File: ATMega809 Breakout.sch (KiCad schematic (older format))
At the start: 42 parts, among them J1 USB_B_Micro, J2 Conn_01x05, J3 Conn_01x20, J4 Conn_01x12, J5 UPDI, Q1 PJA3438-AU, Q2 PJA3438-AU, Q3 PJA3438-AU, Q4 PJA3438-AU, Q5 PJA3438-AU, SW1 RESET, U1 NCP1117-ADJ_SOT223, U2 ATMEGA809-AF

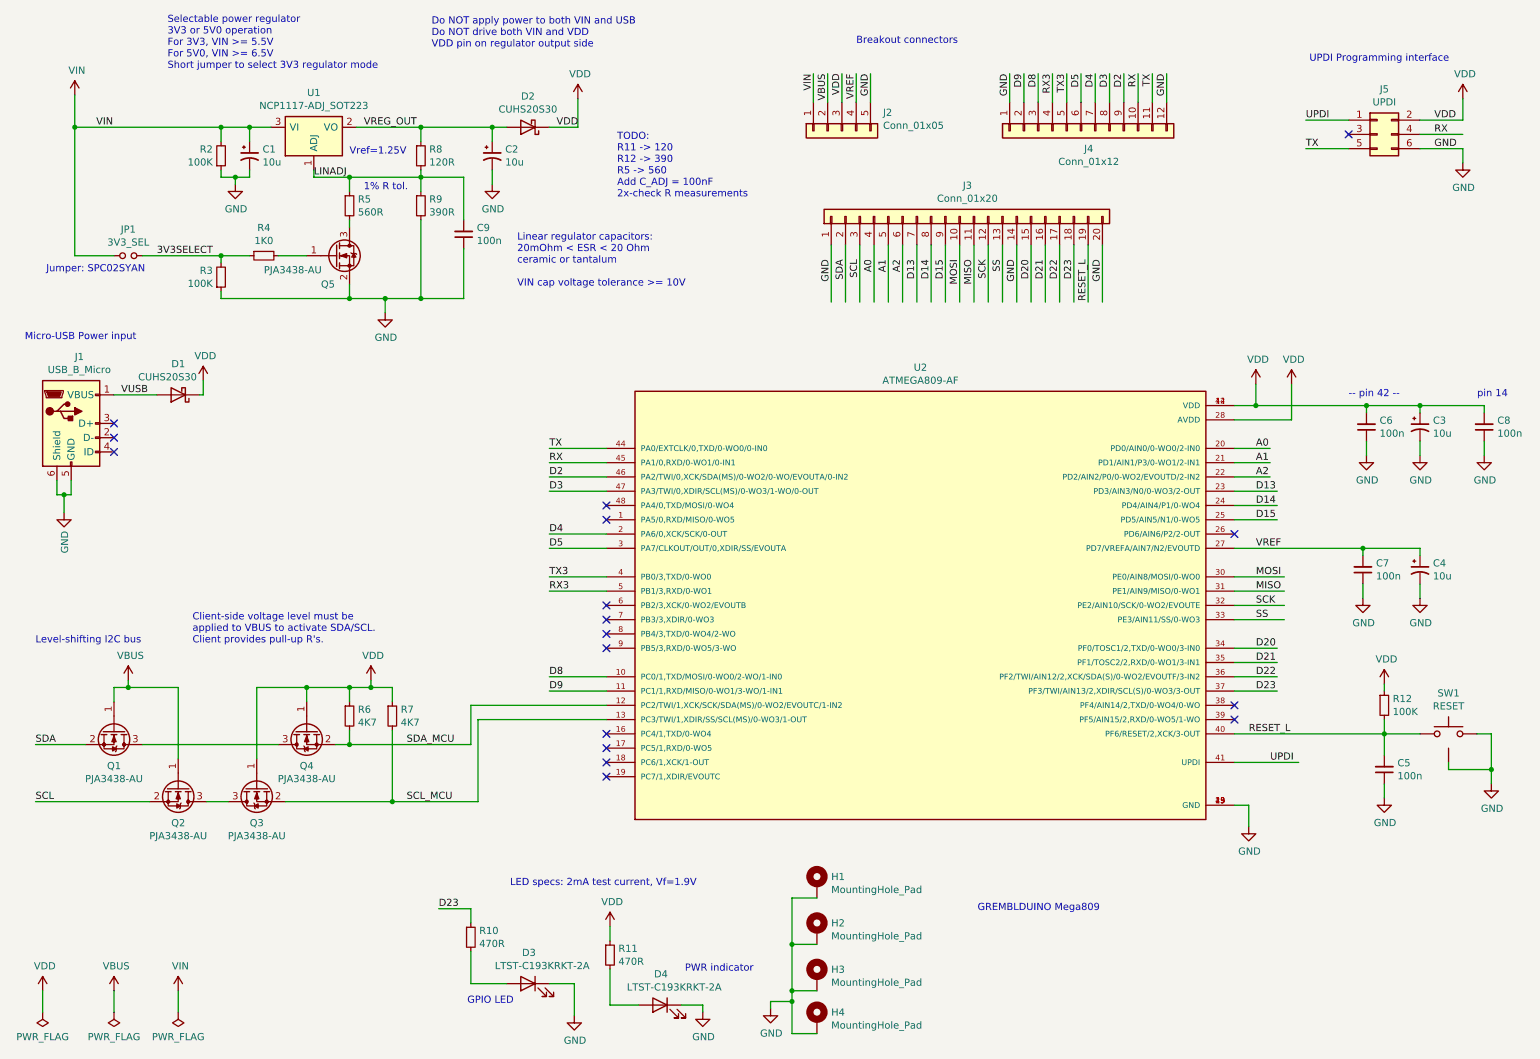
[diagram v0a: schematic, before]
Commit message: Cleanup. Basically ready for mfg.
* Switched USB connectors to pure-SMT assembly, no THT.
* More trace clean-ups. Eliminated 45 deg angles in traces.
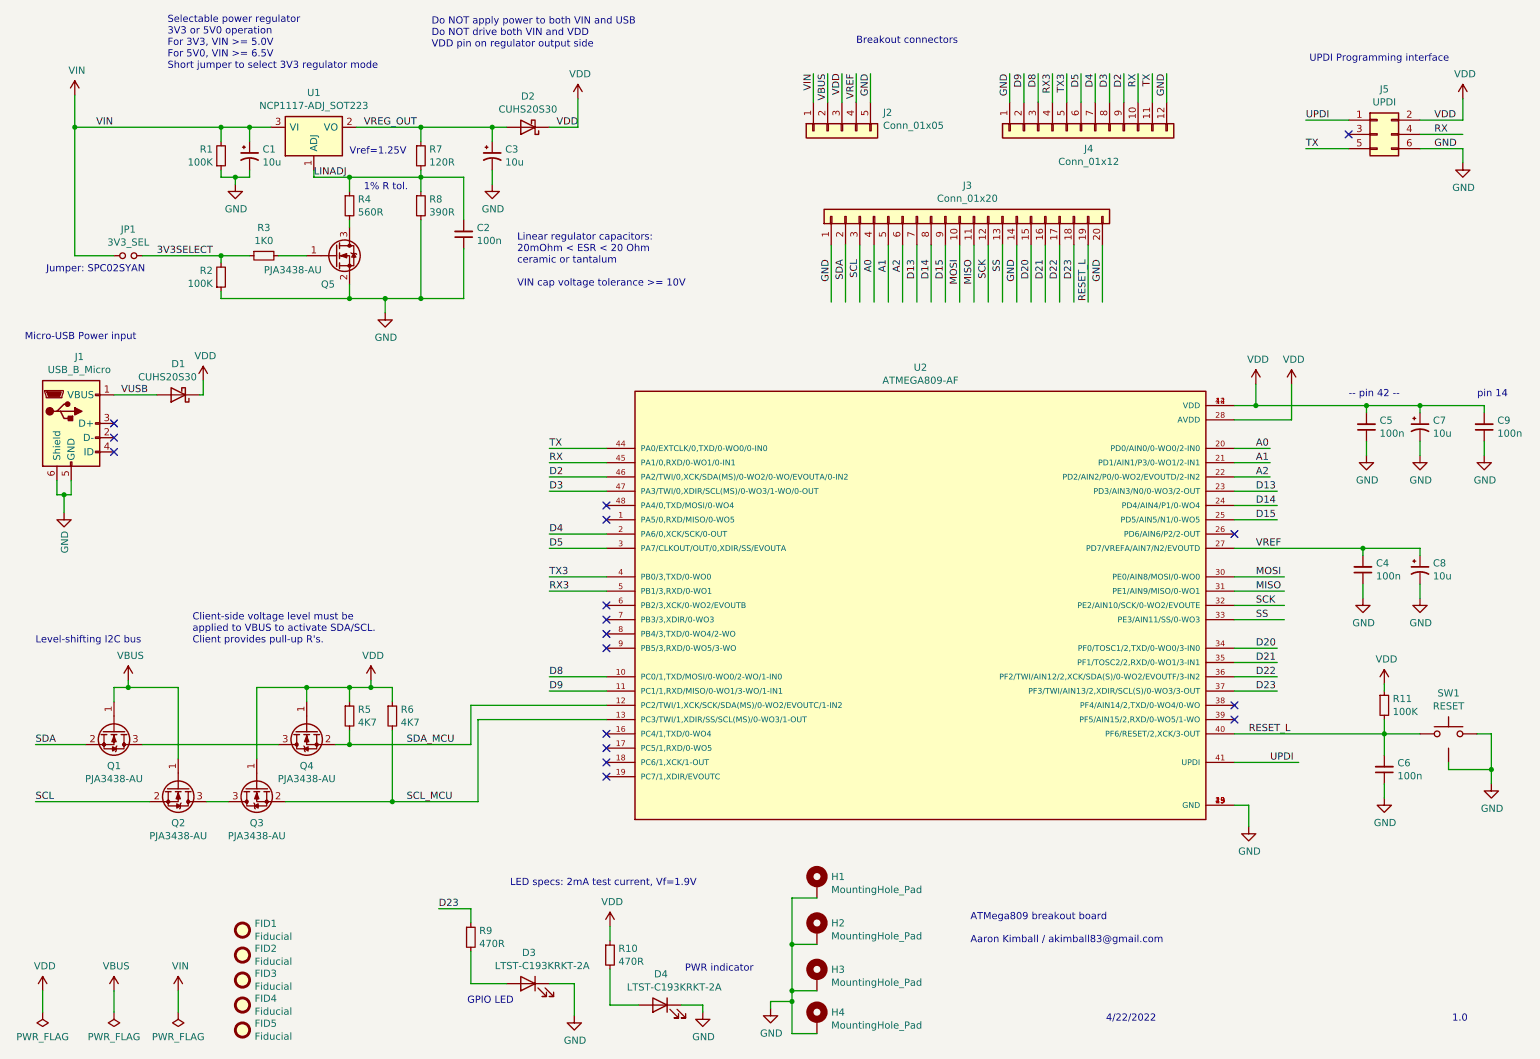
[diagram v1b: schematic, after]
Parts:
- added FID1, FID2, FID3, FID4, FID5: Fiducial, Fiducial:Fiducial_1mm_Mask2mm, symbol Mechanical:Fiducial
- J1: footprint aaron-imported-parts:USB_Micro-B_AdamTech-MCR-B-S-RA-SMT-CS5A-NF -> aaron-imported-parts:USB_Micro-B_Molex_47346-1001; MANUFACTURER Adam Tech -> Molex; MPN MCR-B-S-RA-SMT-CS5A-NF-T/R -> 0473461001
- R4: renamed from R5; MANUFACTURER (none) -> YAEGO; MPN (none) -> RC0603FR-07560RL
- R7: renamed from R8; MPN (none) -> RC0603FR-07120RL
- R8: renamed from R9; MPN (none) -> RC0603FR-07390RL
- U1: footprint Package_TO_SOT_SMD:SOT-223-3_TabPin2 -> Package_TO_SOT_SMD:SOT-223
- renumbered C9 to C2, C2 to C3, C7 to C4, C6 to C5, C5 to C6, C3 to C7, C4 to C8, C8 to C9, R2 to R1, R11 to R10, R12 to R11, R3 to R2, R4 to R3, R6 to R5, R7 to R6, R10 to R9
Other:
- note added: "1.0"
- note added: "4/22/2022"
- note added: "ATMega809 breakout board\n\nAaron Kimball / akimball83@gmail.com"
- note added: "Selectable power regulator\n3V3 or 5V0 operation\nFor 3V3, VIN >= 5.0V\nFor 5V0, VIN >= 6.5V\nShort jumper to select 3V3 regulator mode\n"
- note removed: "GREMBLDUINO Mega809"
- note removed: "Selectable power regulator\n3V3 or 5V0 operation\nFor 3V3, VIN >= 5.5V\nFor 5V0, VIN >= 6.5V\nShort jumper to select 3V3 regulator mode\n"
- note removed: "TODO: \nR11 -> 120\nR12 -> 390\nR5 -> 560\nAdd C_ADJ = 100nF\n2x-check R measurements"

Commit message: Improved RESET circuitry.
* Switch SW1 now discharges capacitor C6 to GND thru R12 (1K0) rather
  than short-circuit.
* Added resistor R13 (1K0) between RESET_L and pull-up R11/capacitor
  C6/SW1. If an external MCU drives RESET_L low, the capacitor will
  discharge through R13 rather than short circuit, limiting max
  discharge current encountered by the GPIO to 5mA.
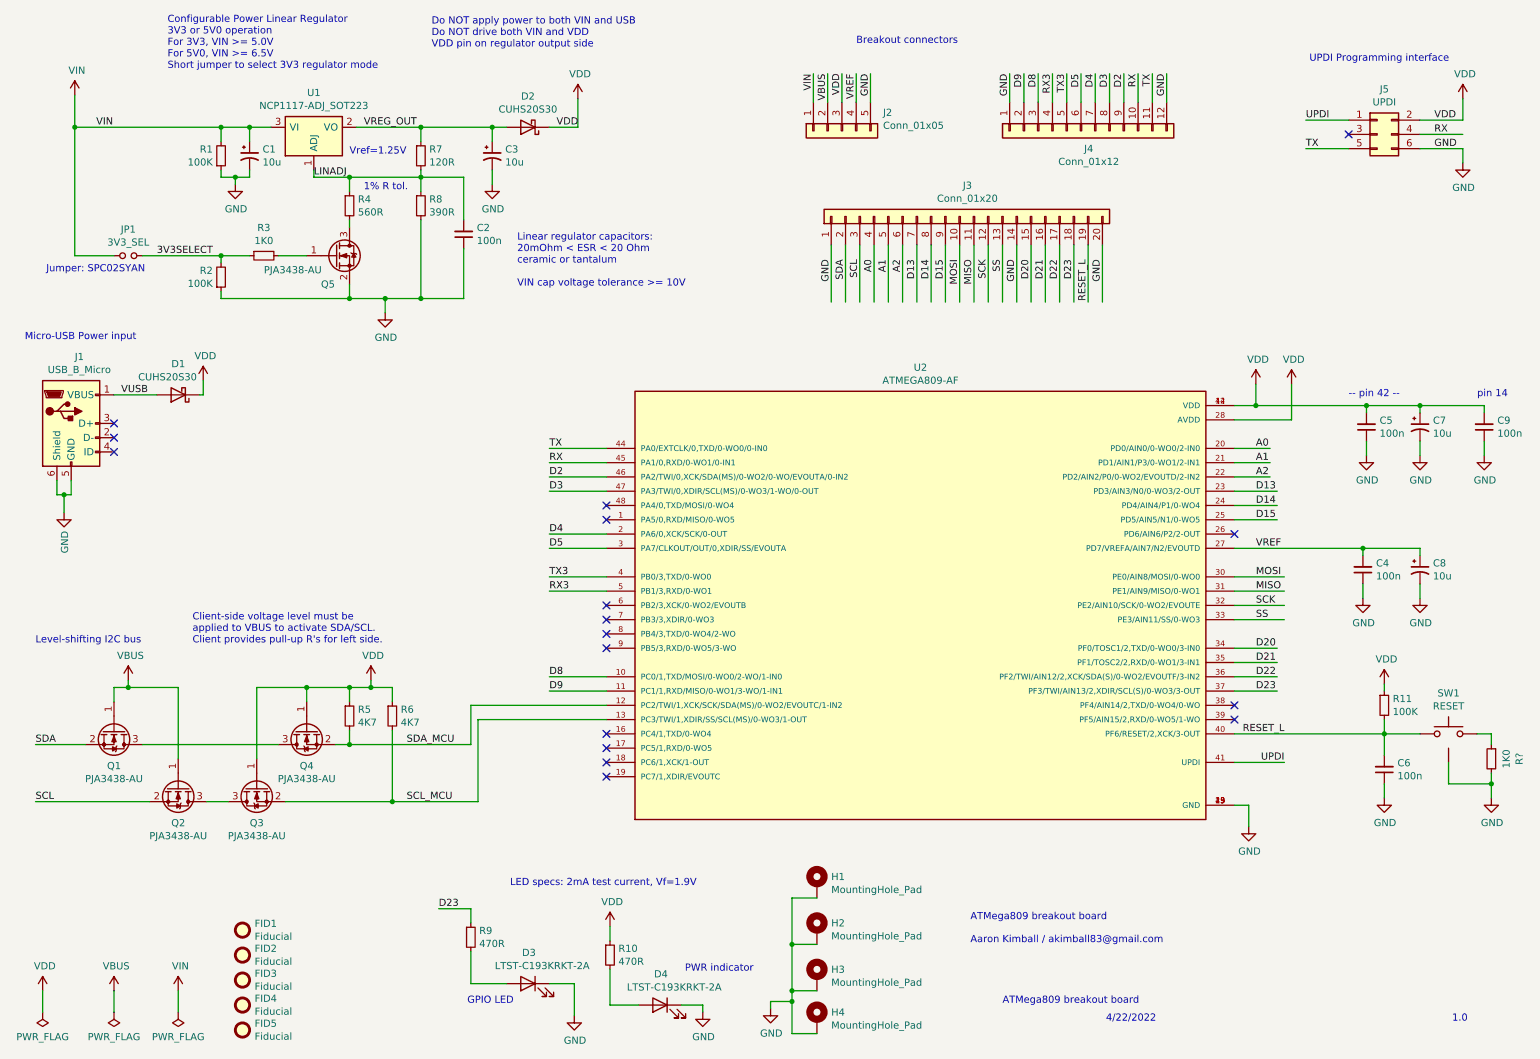
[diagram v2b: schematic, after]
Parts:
- added R?: 1K0, Resistor_SMD:R_0603_1608Metric, symbol Device:R_Small
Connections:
- wire segments 204 -> 205
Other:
- note added: "ATMega809 breakout board"
- note added: "Client-side voltage level must be\napplied to VBUS to activate SDA/SCL.\nClient provides pull-up R's for left side."
- note added: "Configurable Power Linear Regulator\n3V3 or 5V0 operation\nFor 3V3, VIN >= 5.0V\nFor 5V0, VIN >= 6.5V\nShort jumper to select 3V3 regulator mode\n"
- note removed: "Client-side voltage level must be\napplied to VBUS to activate SDA/SCL.\nClient provides pull-up R's."
- note removed: "Selectable power regulator\n3V3 or 5V0 operation\nFor 3V3, VIN >= 5.0V\nFor 5V0, VIN >= 6.5V\nShort jumper to select 3V3 regulator mode\n"
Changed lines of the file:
@@
 Wire Wire Line
 	10650 1500 10650 1600
-Wire Wire Line
-	9050 5800 9500 5800
-Text Label 9300 5800 0    50   ~ 0
+Text Label 9400 5800 2    50   ~ 0
 UPDI
-Text Label 9150 5600 0    50   ~ 0
+Text Label 9400 5600 2    50   ~ 0
 RESET_L
 $Comp
@@
 L power:GND #PWR029
 U 1 1 625DACF2
-P 10850 5950
-F 0 "#PWR029" H 10850 5700 50  0001 C CNN
-F 1 "GND" H 10855 5777 50  0000 C CNN
-F 2 "" H 10850 5950 50  0001 C CNN
-F 3 "" H 10850 5950 50  0001 C CNN
-	1    10850 5950
+P 10850 6050
+F 0 "#PWR029" H 10850 5800 50  0001 C CNN
+F 1 "GND" H 10855 5877 50  0000 C CNN
+F 2 "" H 10850 6050 50  0001 C CNN
+F 3 "" H 10850 6050 50  0001 C CNN
+	1    10850 6050
 	1    0    0    -1
 $EndComp
@@
 $EndComp
 Text Notes 1575 950  0    50   ~ 0
-Selectable power regulator\n3V3 or 5V0 operation\nFor 3V3, VIN >= 5.0V\nFor 5V0, VIN >= 6.5V\nShort jumper to select 3V3 regulator mode\n
+Configurable Power Linear Regulator\n3V3 or 5V0 operation\nFor 3V3, VIN >= 5.0V\nFor 5V0, VIN >= 6.5V\nShort jumper to select 3V3 regulator mode\n
 $Comp
 L power:GND #PWR011
@@
 Connection ~ 3150 6075
 Text Notes 1750 4975 0    50   ~ 0
-Client-side voltage level must be\napplied to VBUS to activate SDA/SCL.\nClient provides pull-up R's.
+Client-side voltage level must be\napplied to VBUS to activate SDA/SCL.\nClient provides pull-up R's for left side.
 Wire Wire Line
 	3000 5275 3150 5275
@@
 GPIO LED
 Wire Wire Line
-	10850 5600 10850 5850
-Wire Wire Line
-	10550 5800 10550 5850
-Wire Wire Line
-	10550 5850 10850 5850
-Connection ~ 10850 5850
-Wire Wire Line
-	10850 5850 10850 5950
+	10550 5950 10850 5950
+Wire Wire Line
+	10850 5950 10850 6050
 $Comp
 L Connector_Generic:Conn_01x05 J2
@@
 Text Notes 8150 7625 0    50   ~ 0
 4/22/2022
+Text Notes 7425 7500 0    50   ~ 0
+ATMega809 breakout board
+$Comp
+L Device:R_Small R?
+U 1 1 62DCA660
+P 10850 5775
+F 0 "R?" V 10654 5775 50  0000 C CNN
+F 1 "1K0" V 10745 5775 50  0000 C CNN
+F 2 "Resistor_SMD:R_0603_1608Metric" H 10850 5775 50  0001 C CNN
+F 3 "~" H 10850 5775 50  0001 C CNN
+F 4 "RC0603FR-071KL" H 10850 5775 50  0001 C CNN "MPN"
+F 5 "YAEGO" H 10850 5775 50  0001 C CNN "MANUFACTURER"
+	1    10850 5775
+	-1   0    0    -1
+$EndComp
+Wire Wire Line
+	10550 5800 10550 5950
+Wire Wire Line
+	10850 5875 10850 5950
+Connection ~ 10850 5950
+Wire Wire Line
+	10850 5675 10850 5600
+Wire Wire Line
+	9400 5800 9050 5800
 $EndSCHEMATC

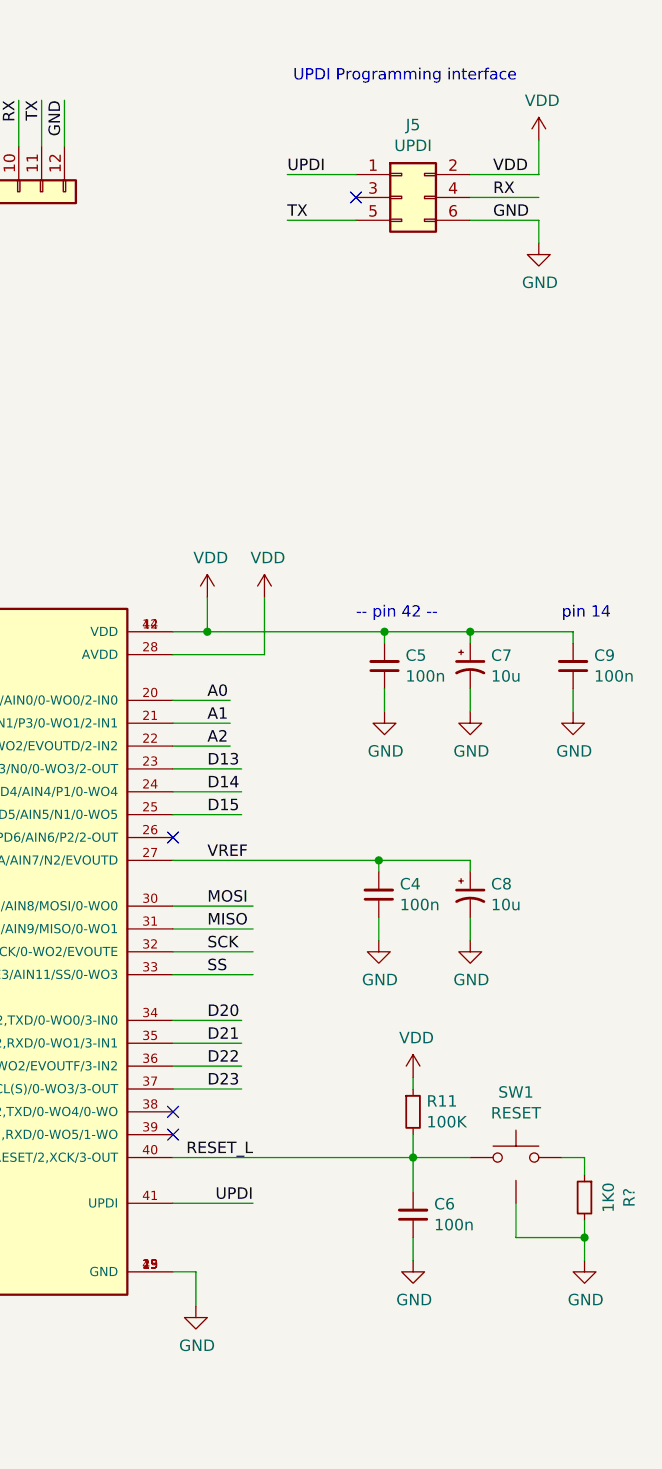
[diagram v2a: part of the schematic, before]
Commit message: Add resistor R14 between UPDI_MCU and UPDI pin.
If the MCU and programmer get out of sync and each try to drive the line
in different directions, somebody's going to have a bad time. Small
resistor ensures device safety while allowing high-speed bandwidth.
Value is sufficiently low that even if the programmer also has a 470R
on the line the logic levels will still work OK.

See discussion:
https://github.com/SpenceKonde/AVR-Guidance/blob/master/HardwareNotes/UPDISeriesResistors.md
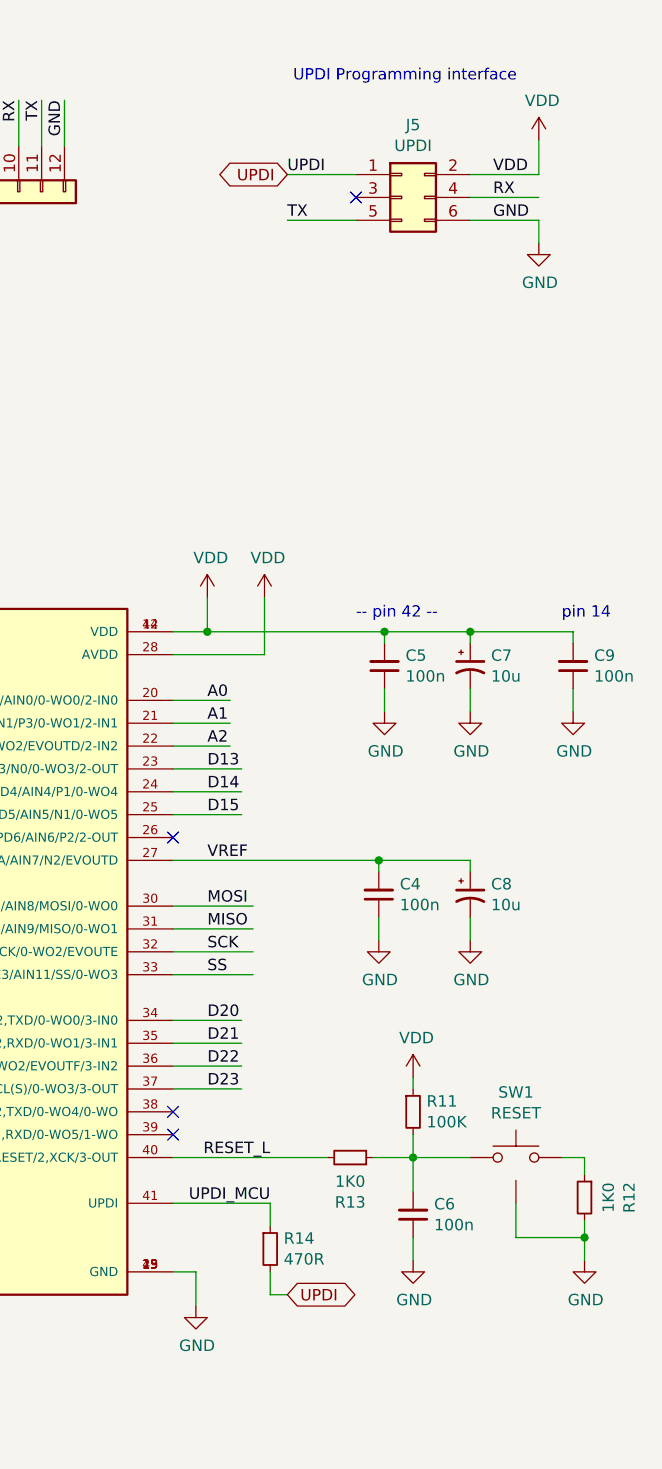
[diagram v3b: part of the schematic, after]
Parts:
- added R13: 1K0, Resistor_SMD:R_0603_1608Metric, symbol Device:R_Small
- added R14: 470R, Resistor_SMD:R_0603_1608Metric, symbol Device:R_Small
- gave numbers to parts that had none: 1
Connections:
- net labels added: UPDI_MCU
- wire segments 205 -> 209
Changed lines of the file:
@@
 Wire Wire Line
 	10650 1500 10650 1600
-Text Label 9400 5800 2    50   ~ 0
-UPDI
-Text Label 9400 5600 2    50   ~ 0
+Text Label 9475 5800 2    50   ~ 0
+UPDI_MCU
+Text Label 9475 5600 2    50   ~ 0
 RESET_L
 $Comp
@@
 	9950 4300 9050 4300
 Connection ~ 9950 4300
-Wire Wire Line
-	9050 5600 10100 5600
 $Comp
 L Device:D_Schottky D2
@@
 ATMega809 breakout board
 $Comp
-L Device:R_Small R?
+L Device:R_Small R12
 U 1 1 62DCA660
 P 10850 5775
-F 0 "R?" V 10654 5775 50  0000 C CNN
+F 0 "R12" V 10654 5775 50  0000 C CNN
 F 1 "1K0" V 10745 5775 50  0000 C CNN
 F 2 "Resistor_SMD:R_0603_1608Metric" H 10850 5775 50  0001 C CNN
@@
 Wire Wire Line
 	10850 5675 10850 5600
-Wire Wire Line
-	9400 5800 9050 5800
+$Comp
+L Device:R_Small R13
+U 1 1 62E3EAED
+P 9825 5600
+F 0 "R13" V 9629 5600 50  0000 C CNN
+F 1 "1K0" V 9720 5600 50  0000 C CNN
+F 2 "Resistor_SMD:R_0603_1608Metric" H 9825 5600 50  0001 C CNN
+F 3 "~" H 9825 5600 50  0001 C CNN
+F 4 "RC0603FR-071KL" H 9825 5600 50  0001 C CNN "MPN"
+F 5 "YAEGO" H 9825 5600 50  0001 C CNN "MANUFACTURER"
+	1    9825 5600
+	0    1    -1   0
+$EndComp
+Wire Wire Line
+	9925 5600 10100 5600
+Wire Wire Line
+	9725 5600 9050 5600
+$Comp
+L Device:R_Small R14
+U 1 1 62F25998
+P 9475 6000
+F 0 "R14" H 9534 6046 50  0000 L CNN
+F 1 "470R" H 9534 5955 50  0000 L CNN
+F 2 "Resistor_SMD:R_0603_1608Metric" H 9475 6000 50  0001 C CNN
+F 3 "~" H 9475 6000 50  0001 C CNN
+F 4 "RC0603FR-07470RL" H 9475 6000 50  0001 C CNN "MPN"
+F 5 "YAEGO" H 9475 6000 50  0001 C CNN "MANUFACTURER"
+	1    9475 6000
+	1    0    0    -1
+$EndComp
+Wire Wire Line
+	9475 5900 9475 5800
+Wire Wire Line
+	9050 5800 9475 5800
+Text GLabel 9550 6200 2    50   BiDi ~ 0
+UPDI
+Wire Wire Line
+	9550 6200 9475 6200
+Wire Wire Line
+	9475 6200 9475 6100
+Text GLabel 9550 1300 0    50   BiDi ~ 0
+UPDI
 $EndSCHEMATC
